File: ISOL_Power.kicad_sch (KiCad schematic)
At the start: 16 parts

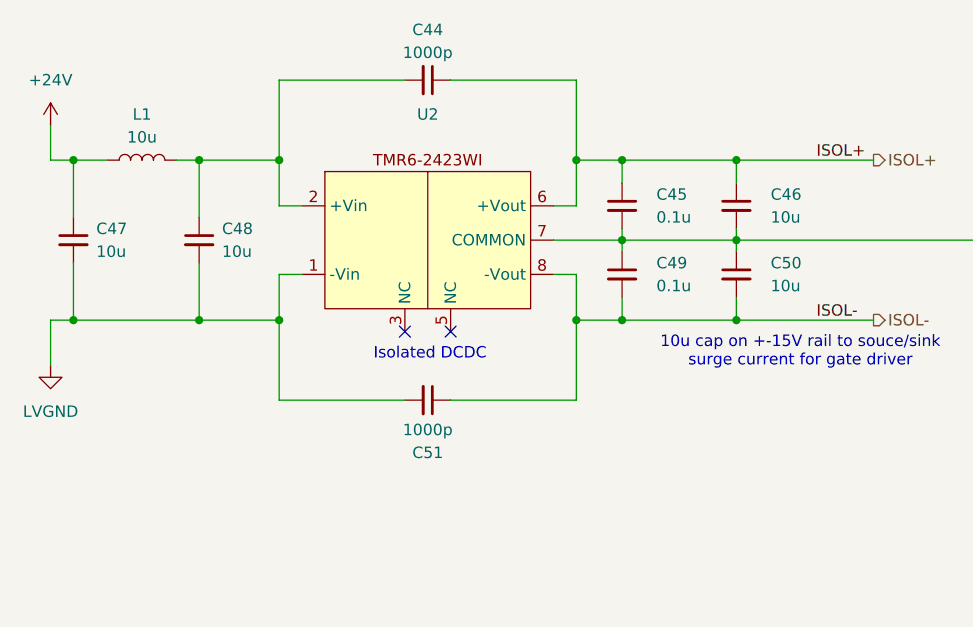
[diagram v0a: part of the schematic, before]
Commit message: new bulk caps, new HV+,- connector placement
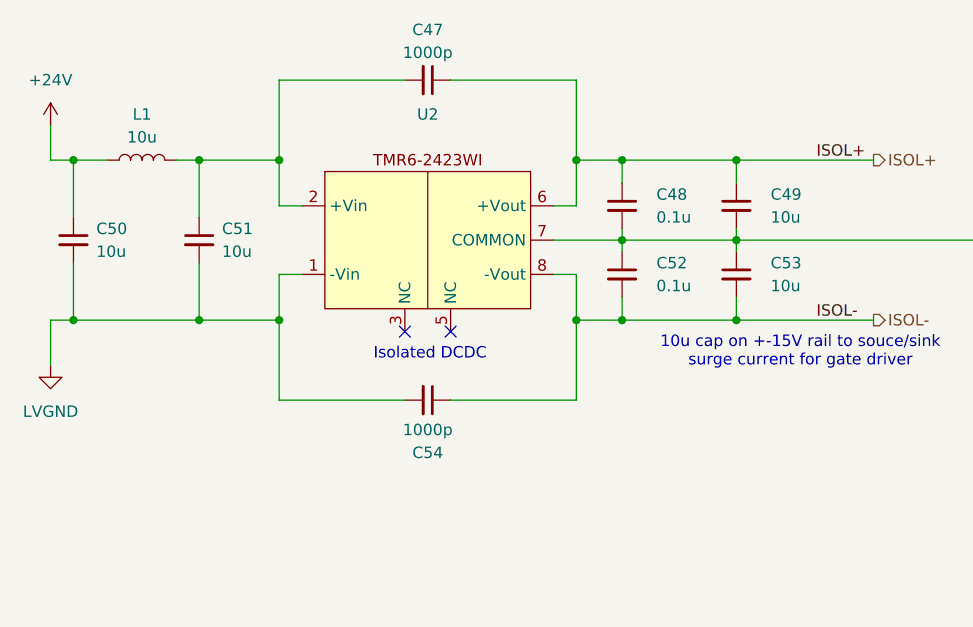
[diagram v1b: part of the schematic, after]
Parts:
- renumbered C44 to C47, C45 to C48, C46 to C49, C47 to C50, C48 to C51, C49 to C52, C50 to C53, C51 to C54
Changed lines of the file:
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@@
 		(on_board yes)
 		(dnp no)
-		(property "Reference" "C49"
+		(property "Reference" "C52"
 			(at 135.89 93.9862 0)
 			(effects
@@
 			(project "TractionInverter"
 				(path "/bc91ffbf-afc6-42bb-9d28-6a3fecc21fcc/77a80145-f9a0-49e1-8a83-585ad4300575"
-					(reference "C49")
+					(reference "C52")
 					(unit 1)
 				)
@@
 		(dnp no)
 		(fields_autoplaced yes)
-		(property "Reference" "#PWR057"
+		(property "Reference" "#PWR063"
 			(at 68.58 111.76 0)
 			(effects
@@
 			(project "TractionInverter"
 				(path "/bc91ffbf-afc6-42bb-9d28-6a3fecc21fcc/77a80145-f9a0-49e1-8a83-585ad4300575"
-					(reference "#PWR057")
+					(reference "#PWR063")
 					(unit 1)
 				)
@@
 		(on_board yes)
 		(dnp no)
-		(property "Reference" "C51"
+		(property "Reference" "C54"
 			(at 110.49 115.062 90)
 			(effects
@@
 			(project "TractionInverter"
 				(path "/bc91ffbf-afc6-42bb-9d28-6a3fecc21fcc/77a80145-f9a0-49e1-8a83-585ad4300575"
-					(reference "C51")
+					(reference "C54")
 					(unit 1)
 				)
@@
 		(on_board yes)
 		(dnp no)
-		(property "Reference" "C44"
+		(property "Reference" "C47"
 			(at 110.49 68.072 90)
 			(effects
@@
 			(project "TractionInverter"
 				(path "/bc91ffbf-afc6-42bb-9d28-6a3fecc21fcc/77a80145-f9a0-49e1-8a83-585ad4300575"
-					(reference "C44")
+					(reference "C47")
 					(unit 1)
 				)
@@
 		(dnp no)
 		(fields_autoplaced yes)
-		(property "Reference" "C48"
+		(property "Reference" "C51"
 			(at 87.63 90.1762 0)
 			(effects
@@
 			(project "TractionInverter"
 				(path "/bc91ffbf-afc6-42bb-9d28-6a3fecc21fcc/77a80145-f9a0-49e1-8a83-585ad4300575"
-					(reference "C48")
+					(reference "C51")
 					(unit 1)
 				)
@@
 		(dnp no)
 		(fields_autoplaced yes)
-		(property "Reference" "#PWR058"
+		(property "Reference" "#PWR064"
 			(at 212.09 111.76 0)
 			(effects
@@
 			(project "TractionInverter"
 				(path "/bc91ffbf-afc6-42bb-9d28-6a3fecc21fcc/77a80145-f9a0-49e1-8a83-585ad4300575"
-					(reference "#PWR058")
+					(reference "#PWR064")
 					(unit 1)
 				)
@@
 		(dnp no)
 		(fields_autoplaced yes)
-		(property "Reference" "C47"
+		(property "Reference" "C50"
 			(at 73.66 90.1762 0)
 			(effects
@@
 			(project "TractionInverter"
 				(path "/bc91ffbf-afc6-42bb-9d28-6a3fecc21fcc/77a80145-f9a0-49e1-8a83-585ad4300575"
-					(reference "C47")
+					(reference "C50")
 					(unit 1)
 				)
@@
 		(dnp no)
 		(fields_autoplaced yes)
-		(property "Reference" "#PWR056"
+		(property "Reference" "#PWR062"
 			(at 177.8 104.14 0)
 			(effects
@@
 			(project "TractionInverter"
 				(path "/bc91ffbf-afc6-42bb-9d28-6a3fecc21fcc/77a80145-f9a0-49e1-8a83-585ad4300575"
-					(reference "#PWR056")
+					(reference "#PWR062")
 					(unit 1)
 				)
@@
 		(on_board yes)
 		(dnp no)
-		(property "Reference" "C46"
+		(property "Reference" "C49"
 			(at 148.59 86.3662 0)
 			(effects
@@
 			(project "TractionInverter"
 				(path "/bc91ffbf-afc6-42bb-9d28-6a3fecc21fcc/77a80145-f9a0-49e1-8a83-585ad4300575"
-					(reference "C46")
+					(reference "C49")
 					(unit 1)
 				)
@@
 		(on_board yes)
 		(dnp no)
-		(property "Reference" "C50"
+		(property "Reference" "C53"
 			(at 148.59 93.9862 0)
 			(effects
@@
 			(project "TractionInverter"
 				(path "/bc91ffbf-afc6-42bb-9d28-6a3fecc21fcc/77a80145-f9a0-49e1-8a83-585ad4300575"
-					(reference "C50")
+					(reference "C53")
 					(unit 1)
 				)
@@
 		(on_board yes)
 		(dnp no)
-		(property "Reference" "C45"
+		(property "Reference" "C48"
 			(at 135.89 86.3662 0)
 			(effects
@@
 			(project "TractionInverter"
 				(path "/bc91ffbf-afc6-42bb-9d28-6a3fecc21fcc/77a80145-f9a0-49e1-8a83-585ad4300575"
-					(reference "C45")
+					(reference "C48")
 					(unit 1)
 				)
@@
 		(dnp no)
 		(fields_autoplaced yes)
-		(property "Reference" "#PWR055"
+		(property "Reference" "#PWR061"
 			(at 68.58 82.55 0)
 			(effects
@@
 			(project "TractionInverter"
 				(path "/bc91ffbf-afc6-42bb-9d28-6a3fecc21fcc/77a80145-f9a0-49e1-8a83-585ad4300575"
-					(reference "#PWR055")
-					(unit 1)
-				)
+					(reference "#PWR061")
+					(unit 1)
+				)

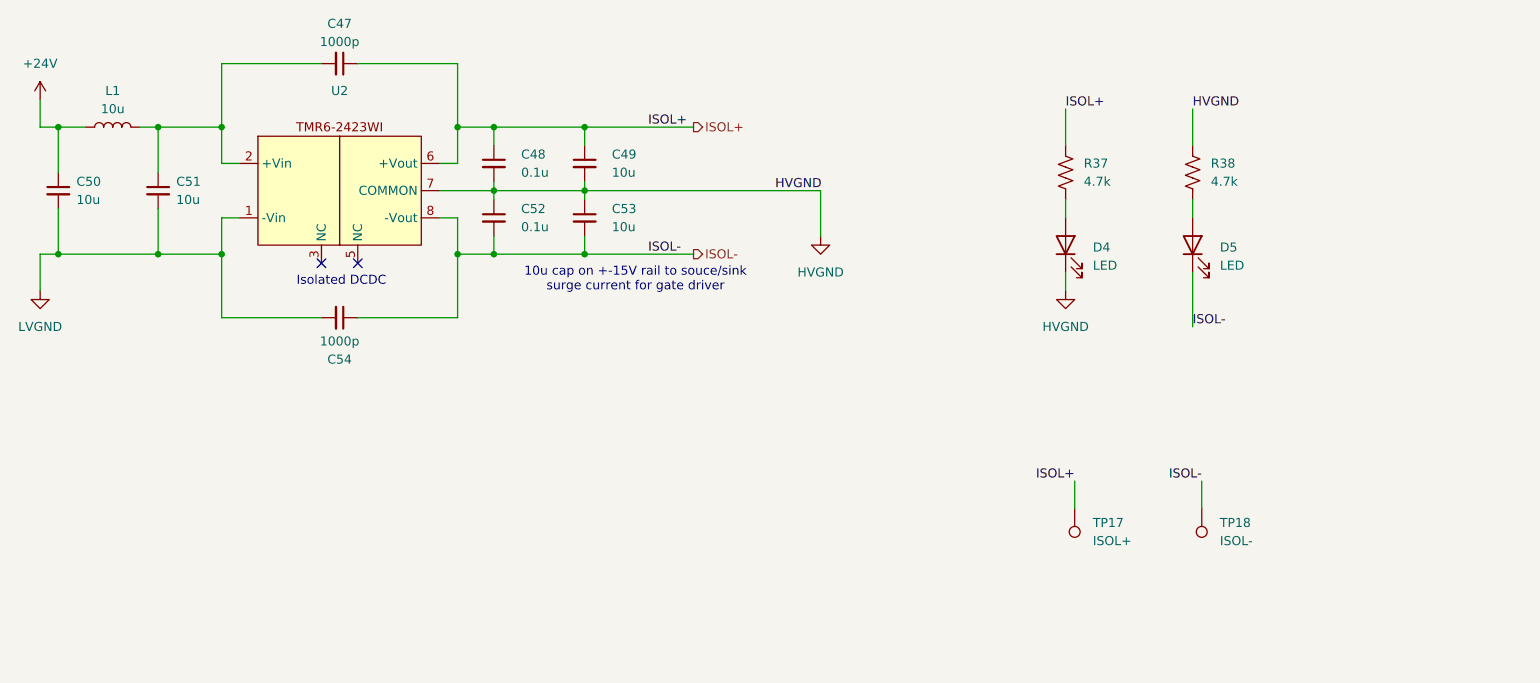
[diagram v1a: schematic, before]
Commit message: killed testpoints
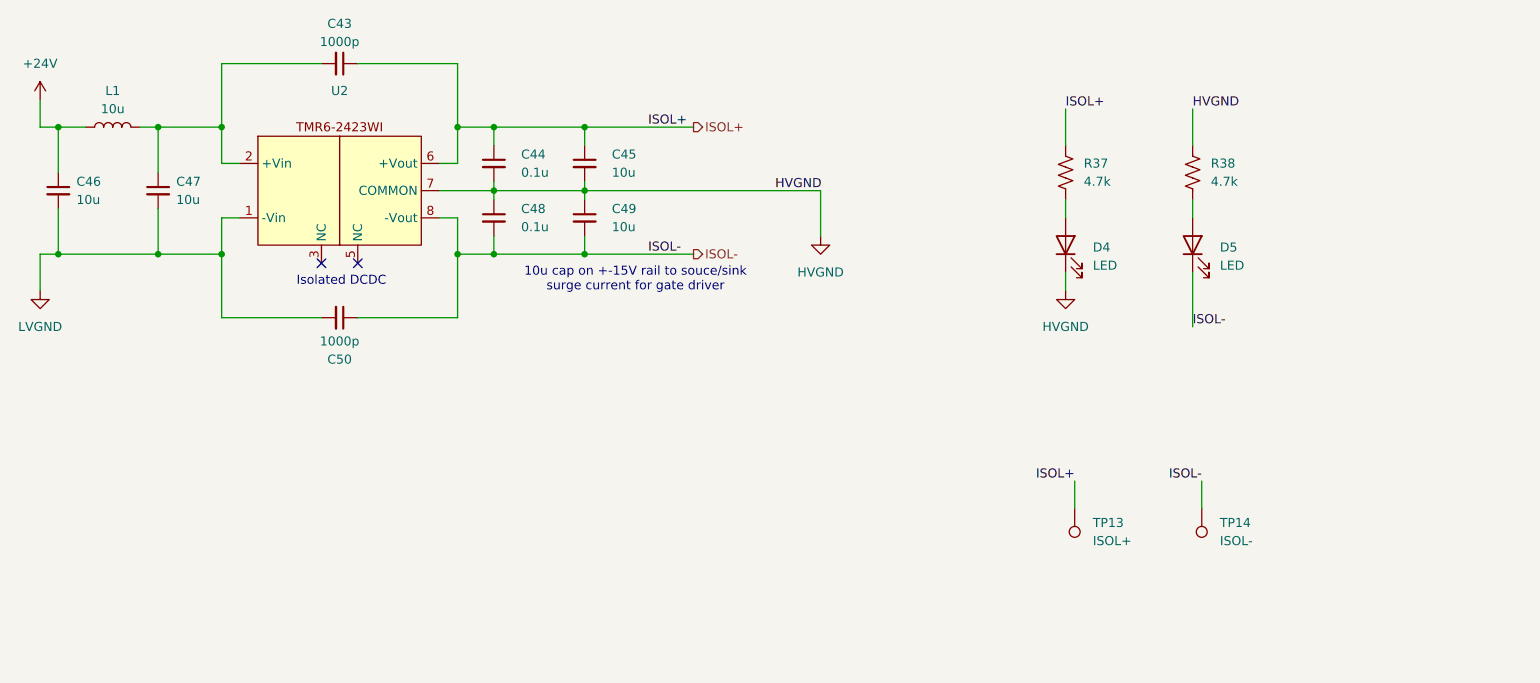
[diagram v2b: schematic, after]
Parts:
- renumbered C47 to C43, C48 to C44, C49 to C45, C50 to C46, C51 to C47, C52 to C48, C53 to C49, C54 to C50, TP17 to TP13, TP18 to TP14
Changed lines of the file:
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@@
 		(dnp no)
 		(fields_autoplaced yes)
-		(property "Reference" "TP18"
+		(property "Reference" "TP14"
 			(at 233.68 137.9219 0)
 			(effects
@@
 			(project "TractionInverter"
 				(path "/bc91ffbf-afc6-42bb-9d28-6a3fecc21fcc/77a80145-f9a0-49e1-8a83-585ad4300575"
-					(reference "TP18")
+					(reference "TP14")
 					(unit 1)
 				)
@@
 		(on_board yes)
 		(dnp no)
-		(property "Reference" "C52"
+		(property "Reference" "C48"
 			(at 135.89 93.9862 0)
 			(effects
@@
 			(project "TractionInverter"
 				(path "/bc91ffbf-afc6-42bb-9d28-6a3fecc21fcc/77a80145-f9a0-49e1-8a83-585ad4300575"
-					(reference "C52")
+					(reference "C48")
 					(unit 1)
 				)
@@
 		(dnp no)
 		(fields_autoplaced yes)
-		(property "Reference" "#PWR063"
+		(property "Reference" "#PWR055"
 			(at 68.58 111.76 0)
 			(effects
@@
 			(project "TractionInverter"
 				(path "/bc91ffbf-afc6-42bb-9d28-6a3fecc21fcc/77a80145-f9a0-49e1-8a83-585ad4300575"
-					(reference "#PWR063")
+					(reference "#PWR055")
 					(unit 1)
 				)
@@
 		(on_board yes)
 		(dnp no)
-		(property "Reference" "C54"
+		(property "Reference" "C50"
 			(at 110.49 115.062 90)
 			(effects
@@
 			(project "TractionInverter"
 				(path "/bc91ffbf-afc6-42bb-9d28-6a3fecc21fcc/77a80145-f9a0-49e1-8a83-585ad4300575"
-					(reference "C54")
+					(reference "C50")
 					(unit 1)
 				)
@@
 		(dnp no)
 		(fields_autoplaced yes)
-		(property "Reference" "TP17"
+		(property "Reference" "TP13"
 			(at 215.9 137.9219 0)
 			(effects
@@
 			(project "TractionInverter"
 				(path "/bc91ffbf-afc6-42bb-9d28-6a3fecc21fcc/77a80145-f9a0-49e1-8a83-585ad4300575"
-					(reference "TP17")
+					(reference "TP13")
 					(unit 1)
 				)
@@
 		(on_board yes)
 		(dnp no)
-		(property "Reference" "C47"
+		(property "Reference" "C43"
 			(at 110.49 68.072 90)
 			(effects
@@
 			(project "TractionInverter"
 				(path "/bc91ffbf-afc6-42bb-9d28-6a3fecc21fcc/77a80145-f9a0-49e1-8a83-585ad4300575"
-					(reference "C47")
+					(reference "C43")
 					(unit 1)
 				)
@@
 		(dnp no)
 		(fields_autoplaced yes)
-		(property "Reference" "C51"
+		(property "Reference" "C47"
 			(at 87.63 90.1762 0)
 			(effects
@@
 			(project "TractionInverter"
 				(path "/bc91ffbf-afc6-42bb-9d28-6a3fecc21fcc/77a80145-f9a0-49e1-8a83-585ad4300575"
-					(reference "C51")
+					(reference "C47")
 					(unit 1)
 				)
@@
 		(dnp no)
 		(fields_autoplaced yes)
-		(property "Reference" "#PWR064"
+		(property "Reference" "#PWR056"
 			(at 212.09 111.76 0)
 			(effects
@@
 			(project "TractionInverter"
 				(path "/bc91ffbf-afc6-42bb-9d28-6a3fecc21fcc/77a80145-f9a0-49e1-8a83-585ad4300575"
-					(reference "#PWR064")
+					(reference "#PWR056")
 					(unit 1)
 				)
@@
 		(dnp no)
 		(fields_autoplaced yes)
-		(property "Reference" "C50"
+		(property "Reference" "C46"
 			(at 73.66 90.1762 0)
 			(effects
@@
 			(project "TractionInverter"
 				(path "/bc91ffbf-afc6-42bb-9d28-6a3fecc21fcc/77a80145-f9a0-49e1-8a83-585ad4300575"
-					(reference "C50")
+					(reference "C46")
 					(unit 1)
 				)
@@
 		(dnp no)
 		(fields_autoplaced yes)
-		(property "Reference" "#PWR062"
+		(property "Reference" "#PWR054"
 			(at 177.8 104.14 0)
 			(effects
@@
 			(project "TractionInverter"
 				(path "/bc91ffbf-afc6-42bb-9d28-6a3fecc21fcc/77a80145-f9a0-49e1-8a83-585ad4300575"
-					(reference "#PWR062")
+					(reference "#PWR054")
 					(unit 1)
 				)
@@
 		(on_board yes)
 		(dnp no)
-		(property "Reference" "C49"
+		(property "Reference" "C45"
 			(at 148.59 86.3662 0)
 			(effects
@@
 			(project "TractionInverter"
 				(path "/bc91ffbf-afc6-42bb-9d28-6a3fecc21fcc/77a80145-f9a0-49e1-8a83-585ad4300575"
-					(reference "C49")
+					(reference "C45")
 					(unit 1)
 				)
@@
 		(on_board yes)
 		(dnp no)
-		(property "Reference" "C53"
+		(property "Reference" "C49"
 			(at 148.59 93.9862 0)
 			(effects
@@
 			(project "TractionInverter"
 				(path "/bc91ffbf-afc6-42bb-9d28-6a3fecc21fcc/77a80145-f9a0-49e1-8a83-585ad4300575"
-					(reference "C53")
+					(reference "C49")
 					(unit 1)
 				)
@@
 		(on_board yes)
 		(dnp no)
-		(property "Reference" "C48"
+		(property "Reference" "C44"
 			(at 135.89 86.3662 0)
 			(effects
@@
 			(project "TractionInverter"
 				(path "/bc91ffbf-afc6-42bb-9d28-6a3fecc21fcc/77a80145-f9a0-49e1-8a83-585ad4300575"
-					(reference "C48")
+					(reference "C44")
 					(unit 1)
 				)
@@
 		(dnp no)
 		(fields_autoplaced yes)
-		(property "Reference" "#PWR061"
+		(property "Reference" "#PWR053"
 			(at 68.58 82.55 0)
 			(effects
@@
 			(project "TractionInverter"
 				(path "/bc91ffbf-afc6-42bb-9d28-6a3fecc21fcc/77a80145-f9a0-49e1-8a83-585ad4300575"
-					(reference "#PWR061")
-					(unit 1)
-				)
+					(reference "#PWR053")
+					(unit 1)
+				)

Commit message: need to pass drc
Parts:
- added TP15, TP17: ISOL+, TestPoint:TestPoint_Pad_D1.5mm, symbol Connector:TestPoint
- added TP16, TP18: ISOL-, TestPoint:TestPoint_Pad_D1.5mm, symbol Connector:TestPoint
- TP13, TP14: footprint TractionInverter:KEYSTONE_5281 -> TestPoint:TestPoint_Pad_D1.5mm
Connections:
- net ISOL+: now also TP15.1, TP17.1
- net ISOL-: now also TP16.1, TP18.1
